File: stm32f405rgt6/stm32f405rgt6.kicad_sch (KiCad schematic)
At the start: 36 parts, among them J1 USART, J2 SWD, J3 I2C, J4 USB_OTG, J5 SPI, J6 AnalogInptus, SW1 SW_Push, SW2 Boot0 selector, U1 USBLC6-2SC6, U2 STM32F405RGT6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

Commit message: tweaked some stuff for the daq and added a files
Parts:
- added J7: 5V, Connector_PinHeader_1.27mm:PinHeader_1x02_P1.27mm_Vertical, symbol Connector:Conn_01x02_Pin
- added J8: CAN, TerminalBlock_Phoenix:TerminalBlock_Phoenix_MKDS-1,5-4_1x04_P5.00mm_Horizontal, symbol Connector:Screw_Terminal_01x04
- added J9: 3.3V, Connector_PinHeader_1.27mm:PinHeader_1x02_P1.27mm_Vertical, symbol Connector:Conn_01x02_Pin
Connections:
- net +3.3V: now also J9.1 (Pin_1)
- net +5V: now also J7.1 (Pin_1), J8.4 (Pin_4)
- net GND: now also J7.2 (Pin_2), J8.1 (Pin_1), J9.2 (Pin_2)
- net CAN_RX: now reaches U2.33 (PB12)
- net CAN_RX: now also J8.3 (Pin_3)
- net CAN_TX: now reaches U2.34 (PB13)
- net CAN_TX: now also J8.2 (Pin_2)
- no-connect marks 36 -> 34
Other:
- note added: "power supply options"

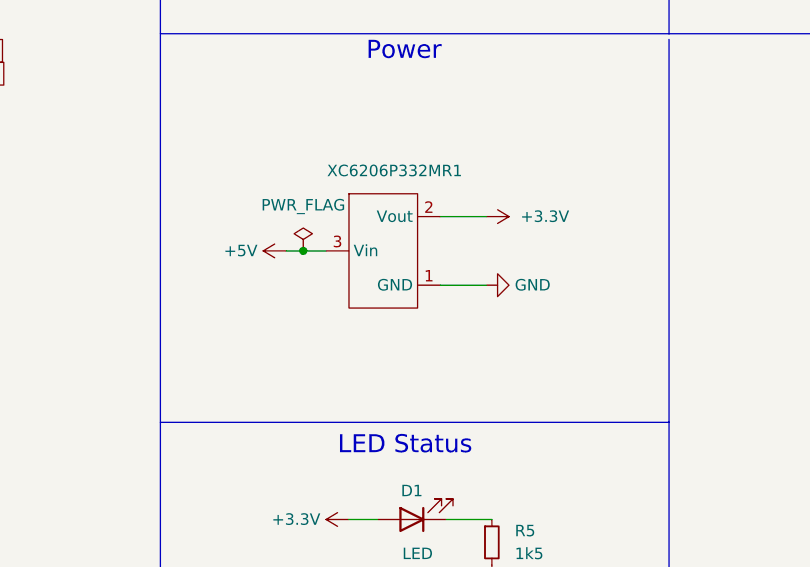
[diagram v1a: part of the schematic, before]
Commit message: added caps to the voltage regulator also gerber and position files need to be updated
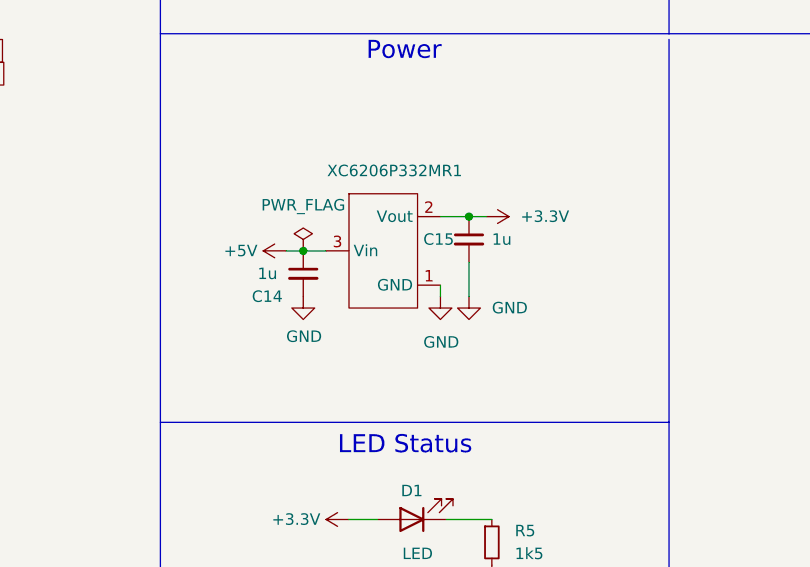
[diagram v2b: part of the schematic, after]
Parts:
- added C14, C15: 1u, Capacitor_SMD:C_0603_1608Metric, symbol Device:C_Small
- J1: footprint Connector_PinHeader_1.27mm:PinHeader_1x04_P1.27mm_Vertical -> Connector_PinHeader_2.54mm:PinHeader_1x04_P2.54mm_Vertical
- J5: footprint TerminalBlock_Phoenix:TerminalBlock_Phoenix_MKDS-1,5-6-5.08_1x06_P5.08mm_Horizontal -> TerminalBlock_Phoenix:TerminalBlock_Phoenix_MKDS-1,5-6_1x06_P5.00mm_Horizontal
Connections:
- net +3.3V: now also C15.1
- net +5V: now also C14.1
- net GND: now also C14.2, C15.2
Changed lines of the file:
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@@
   (junction (at 20.955 72.39) (diameter 0) (color 0 0 0 0)
+  )
+  (junction (at 183.515 120.65) (diameter 0) (color 0 0 0 0)
   )
   (junction (at 41.91 167.64) (diameter 0) (color 0 0 0 0)
@@
     (stroke (width 0) (type default))
   )
-  (wire (pts (xy 180.34 128.27) (xy 185.42 128.27))
-    (stroke (width 0) (type default))
-  )
   (polyline (pts (xy 205.74 143.51) (xy 149.225 143.51))
     (stroke (width 0) (type default))
@@
     (stroke (width 0) (type default))
   )
+  (wire (pts (xy 183.515 129.54) (xy 183.515 125.73))
+    (stroke (width 0) (type default))
+  )
   (wire (pts (xy 22.86 146.685) (xy 45.085 146.685))
     (stroke (width 0) (type default))
@@
     (stroke (width 0) (type default))
   )
+  (wire (pts (xy 183.515 120.65) (xy 185.42 120.65))
+    (stroke (width 0) (type default))
+  )
   (wire (pts (xy 188.595 37.465) (xy 188.595 39.37))
     (stroke (width 0) (type default))
@@
     (stroke (width 0) (type default))
   )
+  (wire (pts (xy 180.34 129.54) (xy 180.34 128.27))
+    (stroke (width 0) (type default))
+  )
   (wire (pts (xy 99.06 90.17) (xy 101.6 90.17))
     (stroke (width 0) (type default))
@@
     (stroke (width 0) (type default))
   )
-  (wire (pts (xy 180.34 120.65) (xy 185.42 120.65))
+  (wire (pts (xy 180.34 120.65) (xy 183.515 120.65))
     (stroke (width 0) (type default))
   )
@@
     )
   )
+  (symbol (lib_id "power:GND") (at 165.1 129.54 0) (unit 1)
+    (in_bom yes) (on_board yes) (dnp no)
+    (property "Reference" "#PWR045" (at 165.1 135.89 0)
+      (effects (font (size 1.27 1.27)) hide)
+    )
+    (property "Value" "GND" (at 163.195 133.985 0)
+      (effects (font (size 1.27 1.27)) (justify left))
+    )
+    (property "Footprint" "" (at 165.1 129.54 0)
+      (effects (font (size 1.27 1.27)) hide)
+    )
+    (property "Datasheet" "" (at 165.1 129.54 0)
+      (effects (font (size 1.27 1.27)) hide)
+    )
+    (pin "1")
+    (instances
+      (project "stm32f405rgt6"
+        (path "/521c39b3-5842-46c1-bbd0-ab8aad1ee68c"
+          (reference "#PWR045") (unit 1)
+        )
+      )
+    )
+  )
   (symbol (lib_id "Custom:XC6206P332MR") (at 173.99 124.46 0) (unit 1)
     (in_bom yes) (on_board yes) (dnp no) (fields_autoplaced)
@@
       (effects (font (size 1.27 1.27)))
     )
-    (property "Footprint" "Connector_PinHeader_1.27mm:PinHeader_1x04_P1.27mm_Vertical" (at 24.765 37.465 0)
+    (property "Footprint" "Connector_PinHeader_2.54mm:PinHeader_1x04_P2.54mm_Vertical" (at 24.765 37.465 0)
       (effects (font (size 1.27 1.27)) hide)
     )
@@
     )
   )
-  (symbol (lib_id "power:GND") (at 185.42 128.27 90) (unit 1)
-    (in_bom yes) (on_board yes) (dnp no) (fields_autoplaced)
-    (property "Reference" "#PWR025" (at 191.77 128.27 0)
-      (effects (font (size 1.27 1.27)) hide)
-    )
-    (property "Value" "GND" (at 188.595 128.27 90)
-      (effects (font (size 1.27 1.27)) (justify right))
-    )
-    (property "Footprint" "" (at 185.42 128.27 0)
-      (effects (font (size 1.27 1.27)) hide)
-    )
-    (property "Datasheet" "" (at 185.42 128.27 0)
+  (symbol (lib_id "power:GND") (at 180.34 129.54 0) (unit 1)
+    (in_bom yes) (on_board yes) (dnp no)
+    (property "Reference" "#PWR025" (at 180.34 135.89 0)
+      (effects (font (size 1.27 1.27)) hide)
+    )
+    (property "Value" "GND" (at 178.435 134.62 0)
+      (effects (font (size 1.27 1.27)) (justify left))
+    )
+    (property "Footprint" "" (at 180.34 129.54 0)
+      (effects (font (size 1.27 1.27)) hide)
+    )
+    (property "Datasheet" "" (at 180.34 129.54 0)
       (effects (font (size 1.27 1.27)) hide)
     )
@@
         (path "/521c39b3-5842-46c1-bbd0-ab8aad1ee68c"
           (reference "C4") (unit 1)
+        )
+      )
+    )
+  )
+  (symbol (lib_id "Device:C_Small") (at 183.515 123.19 0) (unit 1)
+    (in_bom yes) (on_board yes) (dnp no)
+    (property "Reference" "C15" (at 178.435 123.19 0)
+      (effects (font (size 1.27 1.27)) (justify left))
+    )
+    (property "Value" "1u" (at 186.055 123.19 0)
+      (effects (font (size 1.27 1.27)) (justify left))
+    )
+    (property "Footprint" "Capacitor_SMD:C_0603_1608Metric" (at 183.515 123.19 0)
+      (effects (font (size 1.27 1.27)) hide)
+    )
+    (property "Datasheet" "~" (at 183.515 123.19 0)
+      (effects (font (size 1.27 1.27)) hide)
+    )
+    (pin "1")
+    (pin "2")
+    (instances
+      (project "stm32f405rgt6"
+        (path "/521c39b3-5842-46c1-bbd0-ab8aad1ee68c"
+          (reference "C15") (unit 1)
         )
       )
@@
     )
   )
+  (symbol (lib_id "Device:C_Small") (at 165.1 127 0) (unit 1)
+    (in_bom yes) (on_board yes) (dnp no)
+    (property "Reference" "C14" (at 159.385 129.54 0)
+      (effects (font (size 1.27 1.27)) (justify left))
+    )
+    (property "Value" "1u" (at 160.02 127 0)
+      (effects (font (size 1.27 1.27)) (justify left))
+    )
+    (property "Footprint" "Capacitor_SMD:C_0603_1608Metric" (at 165.1 127 0)
+      (effects (font (size 1.27 1.27)) hide)
+    )
+    (property "Datasheet" "~" (at 165.1 127 0)
+      (effects (font (size 1.27 1.27)) hide)
+    )
+    (pin "1")
+    (pin "2")
+    (instances
+      (project "stm32f405rgt6"
+        (path "/521c39b3-5842-46c1-bbd0-ab8aad1ee68c"
+          (reference "C14") (unit 1)
+        )
+      )
+    )
+  )
   (symbol (lib_id "Connector:USB_OTG") (at 95.885 40.64 0) (unit 1)
     (in_bom yes) (on_board yes) (dnp no) (fields_autoplaced)
@@
     )
   )
+  (symbol (lib_id "power:GND") (at 183.515 129.54 0) (unit 1)
+    (in_bom yes) (on_board yes) (dnp no) (fields_autoplaced)
+    (property "Reference" "#PWR041" (at 183.515 135.89 0)
+      (effects (font (size 1.27 1.27)) hide)
+    )
+    (property "Value" "GND" (at 186.055 130.81 0)
+      (effects (font (size 1.27 1.27)) (justify left))
+    )
+    (property "Footprint" "" (at 183.515 129.54 0)
+      (effects (font (size 1.27 1.27)) hide)
+    )
+    (property "Datasheet" "" (at 183.515 129.54 0)
+      (effects (font (size 1.27 1.27)) hide)
+    )
+    (pin "1")
+    (instances
+      (project "stm32f405rgt6"
+        (path "/521c39b3-5842-46c1-bbd0-ab8aad1ee68c"
+          (reference "#PWR041") (unit 1)
+        )
+      )
+    )
+  )
   (symbol (lib_id "power:GND") (at 76.2 171.45 0) (unit 1)
     (in_bom yes) (on_board yes) (dnp no) (fields_autoplaced)
@@
       (effects (font (size 1.27 1.27)))
     )
-    (property "Footprint" "TerminalBlock_Phoenix:TerminalBlock_Phoenix_MKDS-1,5-6-5.08_1x06_P5.08mm_Horizontal" (at 58.42 41.91 0)
-      (effects (font (size 1.27 1.27)) hide)
-    )
+    (property "Footprint" "TerminalBlock_Phoenix:TerminalBlock_Phoenix_MKDS-1,5-6_1x06_P5.00mm_Horizontal" (at 58.42 41.91 0)
+      (effects (font (size 1.27 1.27)) hide)
+    )
